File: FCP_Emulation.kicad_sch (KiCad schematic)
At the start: 88 parts, among them J1 Conn_01x10_Female, J2 Conn_01x10_Female, J3 Conn_01x10_Female, J4 Conn_01x02_Female, J5 Conn_01x02_Female, U1 LM2904, U2 LM2904

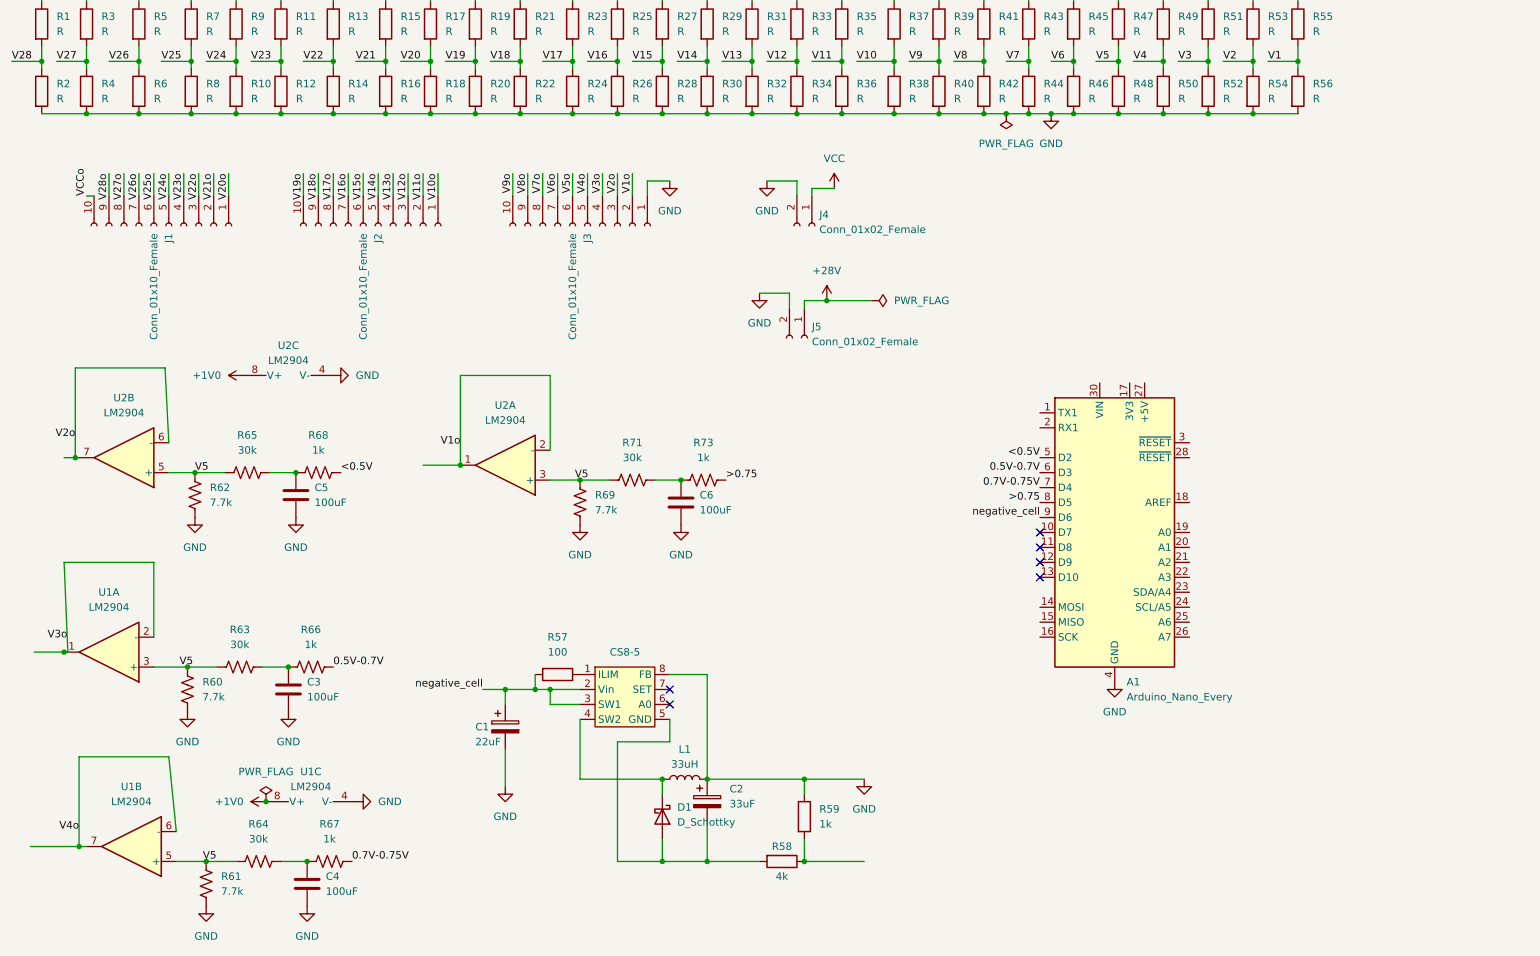
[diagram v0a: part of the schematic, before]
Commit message: updated flags and 5V regulator
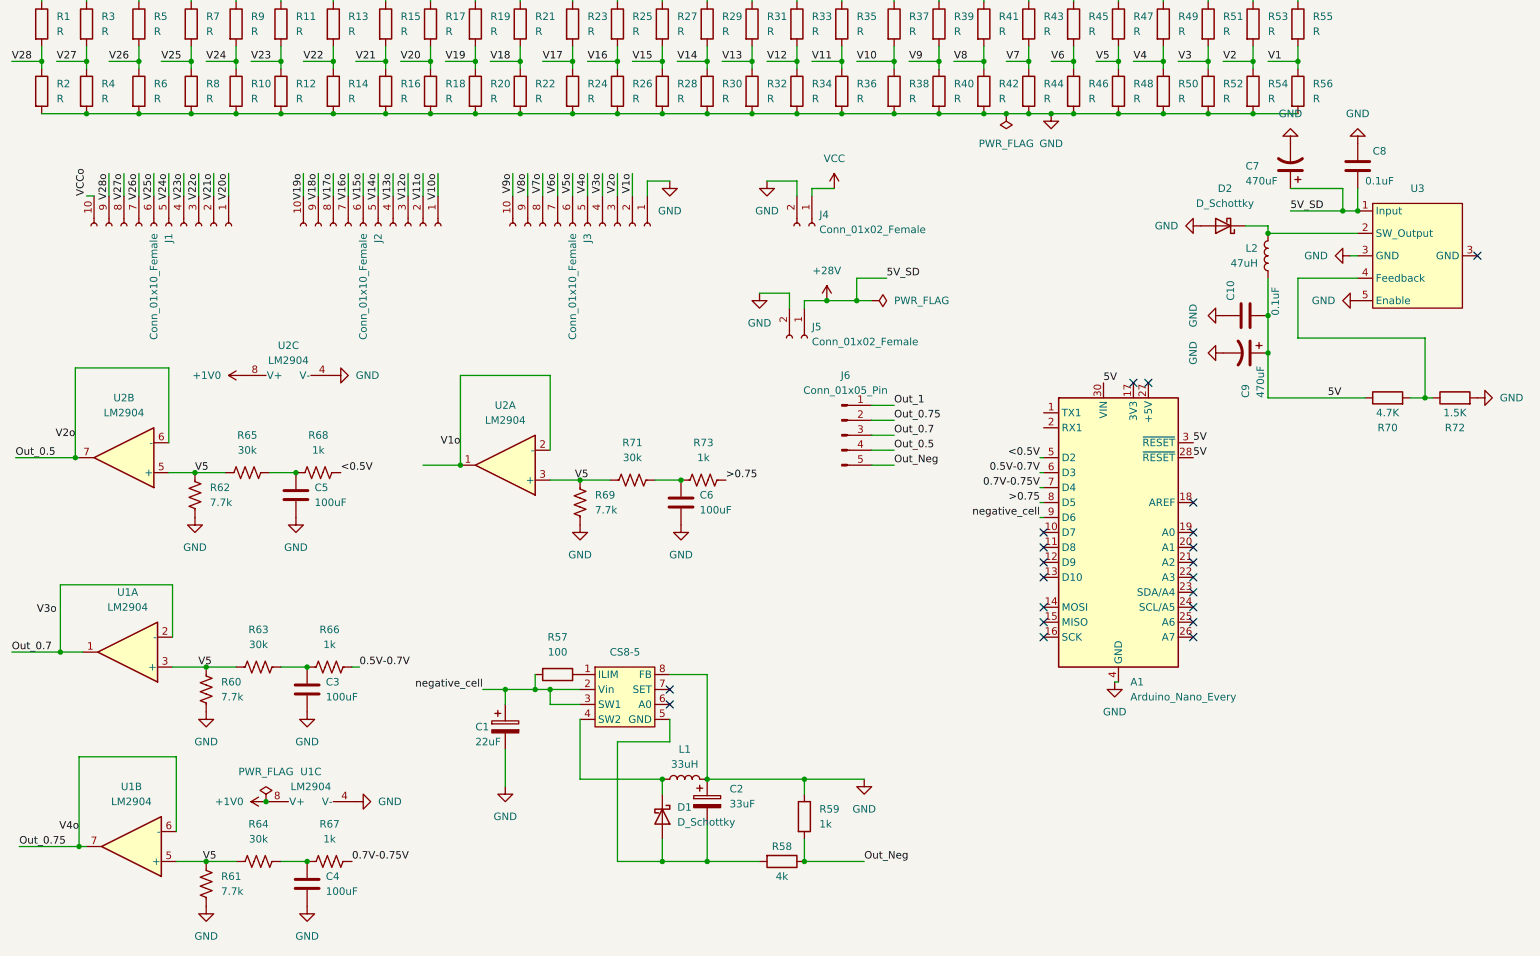
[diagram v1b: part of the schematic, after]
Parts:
- added C10, C8: 0.1uF, symbol Device:C
- added C7, C9: 470uF, symbol Device:C_Polarized_US
- added D2: D_Schottky, symbol Device:D_Schottky
- added J6: Conn_01x05_Pin, symbol Connector:Conn_01x05_Pin
- added L2: 47uH, symbol Device:L
- added R70: 4.7K, symbol Device:R
- added R72: 1.5K, symbol Device:R
- added U3: ~, symbol 36V_to_5V_reg:Buck_Switching_Regulator_IC_Positive_Fixed_5V_1_Output_3A_TO-263-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
- U1, U2: footprint Package_SO:SOIC-8-N7_3.9x4.9mm_P1.27mm -> Package_SO:SOIC-8_3.9x4.9mm_P1.27mm
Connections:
- net +28V: now also C7.1, C8.2, U3.1 (Input)
- net GND: now also C10.1, C7.2, C8.1, C9.2, D2.2 (A), R72.2, U3.3 (GND), U3.5 (Enable)
- net V3o: no longer U1.1, U1.2 (-)
- net Out_Neg: now reaches R58.1, R59.2
- net Out_Neg: now also J6.5 (Pin_5)
- net 5V: now reaches A1.28 (~{RESET})
- net 5V: now also A1.3 (~{RESET}), A1.30 (VIN), C10.2, C9.1, L2.1, R70.1
- net V2o renamed Out_0.5
- net Out_0.5: now also J6.4 (Pin_4)
- net V4o renamed Out_0.75
- net Out_0.75: now also J6.2 (Pin_2)
- new net: D2.1 (K), L2.2, U3.2 (SW_Output)
- new net: R70.2, R72.1, U3.4 (Feedback)
- new net Out_0.7: J6.3 (Pin_3), U1.1, U1.2 (-)
- new net Out_1: J6.1 (Pin_1)
- no-connect marks 6 -> 21
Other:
- moved on the sheet: A1, C3, R60, R63, R66, U1A

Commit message: update
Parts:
- removed J6: Conn_01x05_Pin, symbol Connector:Conn_01x05_Pin
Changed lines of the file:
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@@
     (stroke (width 0) (type default))
   )
-  (wire (pts (xy 163.83 105.41) (xy 160.02 105.41))
-    (stroke (width 0) (type default))
-  )
   (wire (pts (xy 59.69 27.94) (xy 59.69 31.75))
     (stroke (width 0) (type default))
@@
     (stroke (width 0) (type default))
   )
-  (wire (pts (xy 163.83 100.33) (xy 160.02 100.33))
-    (stroke (width 0) (type default))
-  )
   (wire (pts (xy 116.84 157.48) (xy 116.84 177.8))
     (stroke (width 0) (type default))
@@
     (stroke (width 0) (type default))
   )
-  (wire (pts (xy 163.83 110.49) (xy 160.02 110.49))
-    (stroke (width 0) (type default))
-  )
   (wire (pts (xy 41.91 160.02) (xy 25.4 160.02))
     (stroke (width 0) (type default))
@@
     (stroke (width 0) (type default))
   )
-  (wire (pts (xy 163.83 102.87) (xy 160.02 102.87))
-    (stroke (width 0) (type default))
-  )
   (wire (pts (xy 179.07 50.8) (xy 182.88 50.8))
     (stroke (width 0) (type default))
@@
     (stroke (width 0) (type default))
   )
-  (wire (pts (xy 163.83 107.95) (xy 160.02 107.95))
-    (stroke (width 0) (type default))
-  )
   (wire (pts (xy 102.87 146.05) (xy 102.87 148.59))
     (stroke (width 0) (type default))
@@
     (effects (font (size 1.27 1.27)) (justify left bottom))
   )
-  (label "Out_0.75" (at 163.83 102.87 0) (fields_autoplaced)
-    (effects (font (size 1.27 1.27)) (justify left bottom))
-  )
   (label "V5" (at 109.6084 113.03 0) (fields_autoplaced)
     (effects (font (size 1.27 1.27)) (justify left bottom))
@@
     (effects (font (size 1.27 1.27)) (justify right bottom))
   )
-  (label "Out_0.5" (at 163.83 107.95 0) (fields_autoplaced)
-    (effects (font (size 1.27 1.27)) (justify left bottom))
-  )
   (label "V25" (at 39.37 41.91 0) (fields_autoplaced)
     (effects (font (size 1.27 1.27)) (justify left bottom))
@@
     (effects (font (size 1.27 1.27)) (justify right bottom))
   )
-  (label "Out_0.7" (at 163.83 105.41 0) (fields_autoplaced)
-    (effects (font (size 1.27 1.27)) (justify left bottom))
-  )
   (label "V23" (at 54.61 41.91 0) (fields_autoplaced)
     (effects (font (size 1.27 1.27)) (justify left bottom))
@@
     (effects (font (size 1.27 1.27)) (justify right bottom))
   )
-  (label "Out_Neg" (at 163.83 110.49 0) (fields_autoplaced)
-    (effects (font (size 1.27 1.27)) (justify left bottom))
-  )
   (label "negative_cell" (at 188.595 119.38 180) (fields_autoplaced)
     (effects (font (size 1.27 1.27)) (justify right bottom))
@@
     (effects (font (size 1.27 1.27)) (justify left bottom))
   )
-  (label "Out_1" (at 163.83 100.33 0) (fields_autoplaced)
-    (effects (font (size 1.27 1.27)) (justify left bottom))
-  )
   (label "Out_0.75" (at 15.24 175.26 0) (fields_autoplaced)
     (effects (font (size 1.27 1.27)) (justify left bottom))
@@
         )
       )
-    )
-  )
-  (symbol (lib_id "Connector:Conn_01x05_Pin") (at 154.94 105.41 0) (unit 1)
-    (in_bom yes) (on_board yes) (dnp no) (fields_autoplaced)
-    (property "Reference" "J6" (at 155.575 95.25 0)
-      (effects (font (size 1.27 1.27)))
-    )
-    (property "Value" "Conn_01x05_Pin" (at 155.575 97.79 0)
-      (effects (font (size 1.27 1.27)))
-    )
-    (property "Footprint" "" (at 154.94 105.41 0)
-      (effects (font (size 1.27 1.27)) hide)
-    )
-    (property "Datasheet" "~" (at 154.94 105.41 0)
-      (effects (font (size 1.27 1.27)) hide)
-    )
-    (pin "1")
-    (pin "2")
-    (pin "3")
-    (pin "4")
-    (pin "5")
-    (instances
-      (project "FCP_Emulation"
-        (path "/2bfb74c9-fd5c-473a-8e9a-72656c2b9b26"
-          (reference "J6") (unit 1)
-        )
-      )

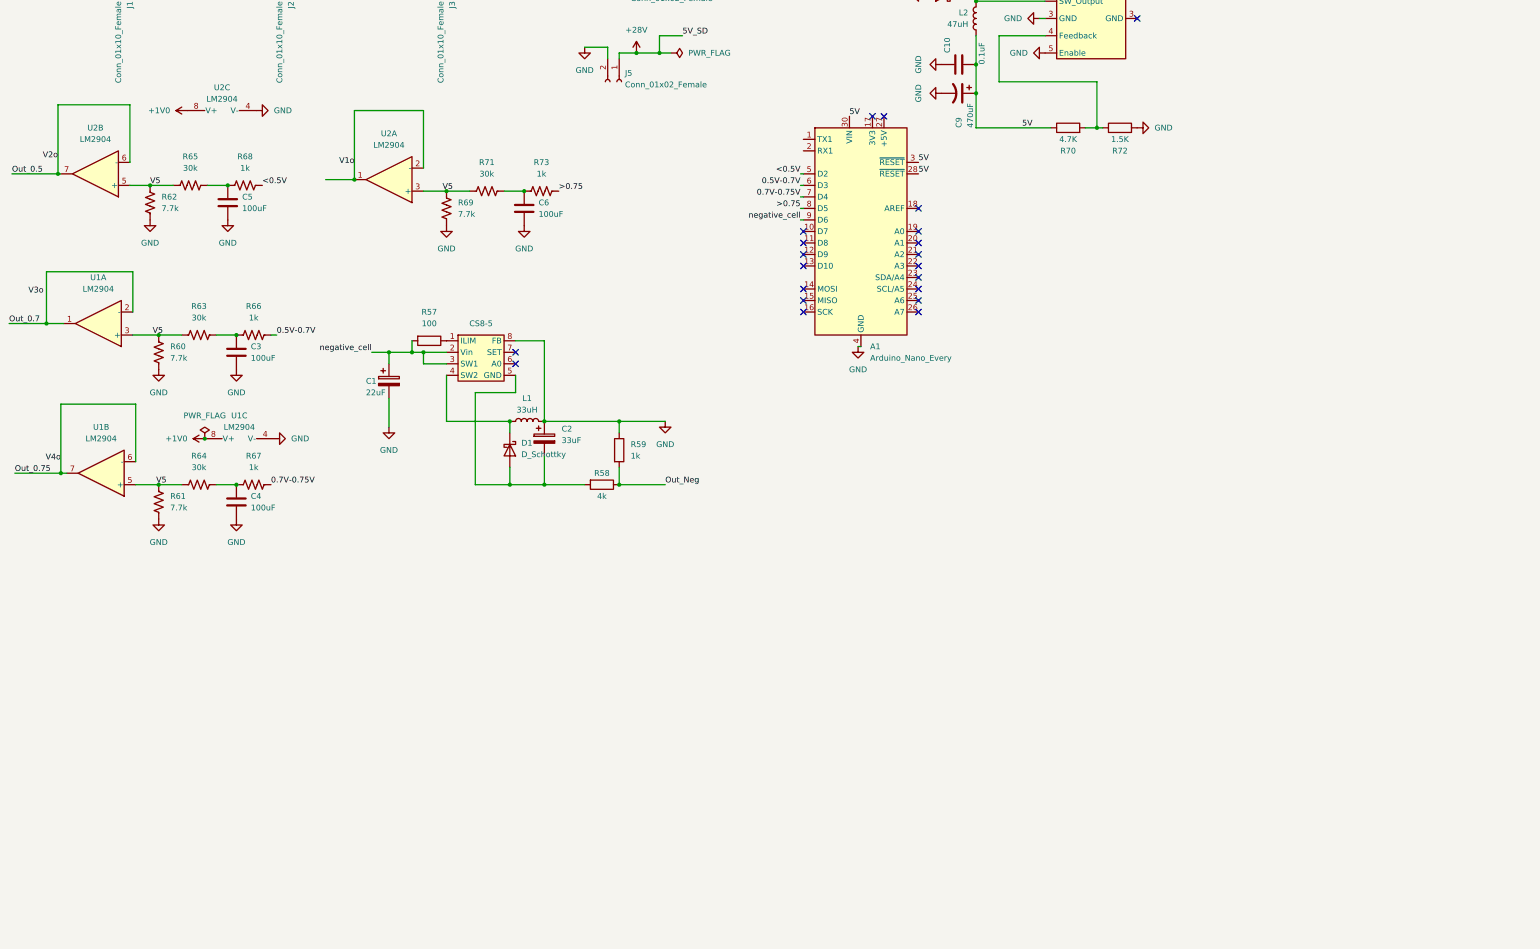
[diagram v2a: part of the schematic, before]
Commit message: re-added buffers and added positive case for the negative case circuit
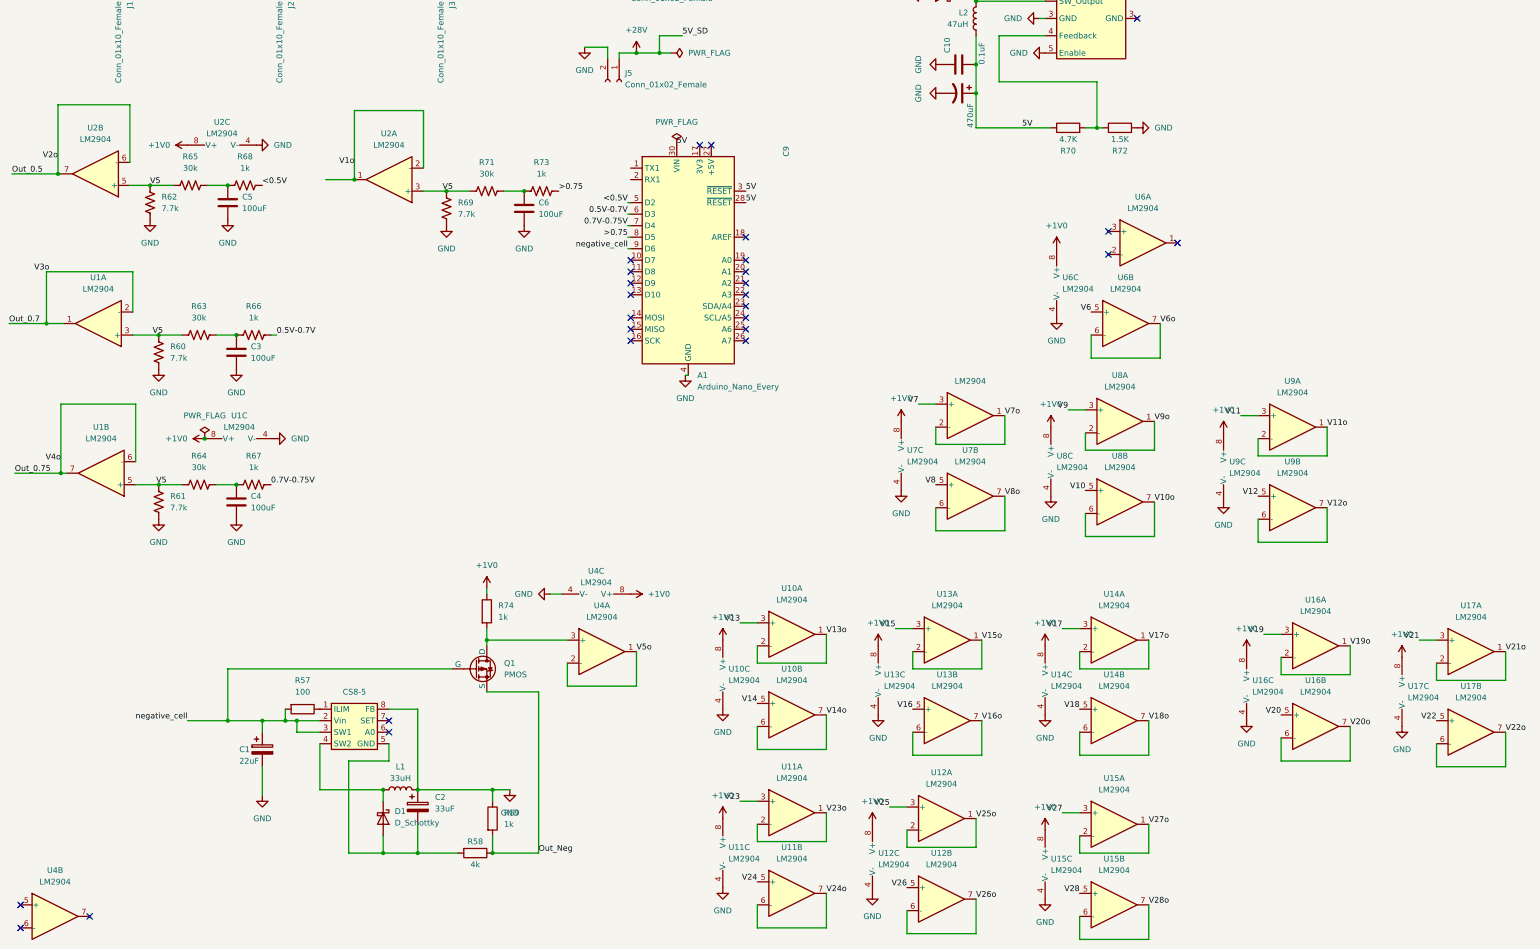
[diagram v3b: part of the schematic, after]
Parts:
- added Q1: PMOS, Package_TO_SOT_SMD:SOT-23-3, symbol Simulation_SPICE:PMOS
- added R74: 1k, Resistor_SMD:R_01005_0402Metric, symbol Device:R
- added U10, U11, U12, U13, U14, U15, U16, U17, U4, U6, U7, U8, U9: LM2904, symbol Amplifier_Operational:LM2904
- C10, C8: footprint (none) -> Capacitor_Tantalum_SMD:CP_EIA-3216-10_Kemet-I
- D2: footprint (none) -> Diode_SMD:D_SMB
- R70: footprint (none) -> Resistor_SMD:R_0402_1005Metric
- U3: footprint (none) -> Package_TO_SOT_SMD:TO-263-6
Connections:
- net V3o is gone; now on net Out_0.7: J3.4 (Pin_4)
- net +1V0: now also R74.1, U10.8 (V+), U11.8 (V+), U12.8 (V+), U13.8 (V+), U14.8 (V+), U15.8 (V+), U16.8 (V+), U17.8 (V+), U4.8 (V+), U6.8 (V+), U7.8 (V+), U8.8 (V+), U9.8 (V+)
- net GND: now also U10.4 (V-), U11.4 (V-), U12.4 (V-), U13.4 (V-), U14.4 (V-), U15.4 (V-), U16.4 (V-), U17.4 (V-), U4.4 (V-), U6.4 (V-), U7.4 (V-), U8.4 (V-), U9.4 (V-)
- net Out_Neg: now also Q1.3 (S)
- net V10: now also U8.5 (+)
- net V10o: now also U8.6 (-), U8.7
- net V11: now also U9.3 (+)
- net V11o: now also U9.1, U9.2 (-)
- net V12: now also U9.5 (+)
- net V12o: now also U9.6 (-), U9.7
- net V13: now also U10.3 (+)
- net V13o: now also U10.1, U10.2 (-)
- net V14: now also U10.5 (+)
- net V14o: now also U10.6 (-), U10.7
- net V15: now also U13.3 (+)
- net V15o: now also U13.1, U13.2 (-)
- net V16: now also U13.5 (+)
- net V16o: now also U13.6 (-), U13.7
- net V17: now also U14.3 (+)
- net V17o: now also U14.1, U14.2 (-)
- net V18: now also U14.5 (+)
- net V18o: now also U14.6 (-), U14.7
- net V19: now also U16.3 (+)
- net V19o: now also U16.1, U16.2 (-)
- net V20: now also U16.5 (+)
- net V20o: now also U16.6 (-), U16.7
- net V21: now also U17.3 (+)
- net V21o: now also U17.1, U17.2 (-)
- net V22: now also U17.5 (+)
- net V22o: now also U17.6 (-), U17.7
- net V23: now also U11.3 (+)
- net V23o: now also U11.1, U11.2 (-)
- net V24: now also U11.5 (+)
- net V24o: now also U11.6 (-), U11.7
- net V25: now also U12.3 (+)
- net V25o: now also U12.1, U12.2 (-)
- net V26: now also U12.5 (+)
- net V26o: now also U12.6 (-), U12.7
- net V27: now also U15.3 (+)
- net V27o: now also U15.1, U15.2 (-)
- net V28: now also U15.5 (+)
- net V28o: now also U15.6 (-), U15.7
- net V5o: now also U4.1, U4.2 (-)
- net V6: now also U6.5 (+)
- net V6o: now also U6.6 (-), U6.7
- net V7: now also U7.3 (+)
- net V7o: now also U7.1, U7.2 (-)
- net V8: now also U7.5 (+)
- net V8o: now also U7.6 (-), U7.7
- net V9: now also U8.3 (+)
- net V9o: now also U8.1, U8.2 (-)
- net negative_cell: now also Q1.2 (G)
- new net: Q1.1 (D), R74.2, U4.3 (+)
- no-connect marks 21 -> 27
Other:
- moved on the sheet: A1, C1, C2, CS8-5, D1, L1, R57, R58, R59, U2C
